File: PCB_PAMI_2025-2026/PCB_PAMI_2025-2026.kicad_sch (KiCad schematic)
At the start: 63 parts, among them J1 BAU, J10 MOTOR 4, J11 COMM_inter_mcu, J12 USB_C_Receptacle_USB2.0_16P, J13 BOOST_OUT, J2 BAT+, J3 VIN_Connector, J4 BAT-, J6 BOOST_IN, J7 MOTOR 3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

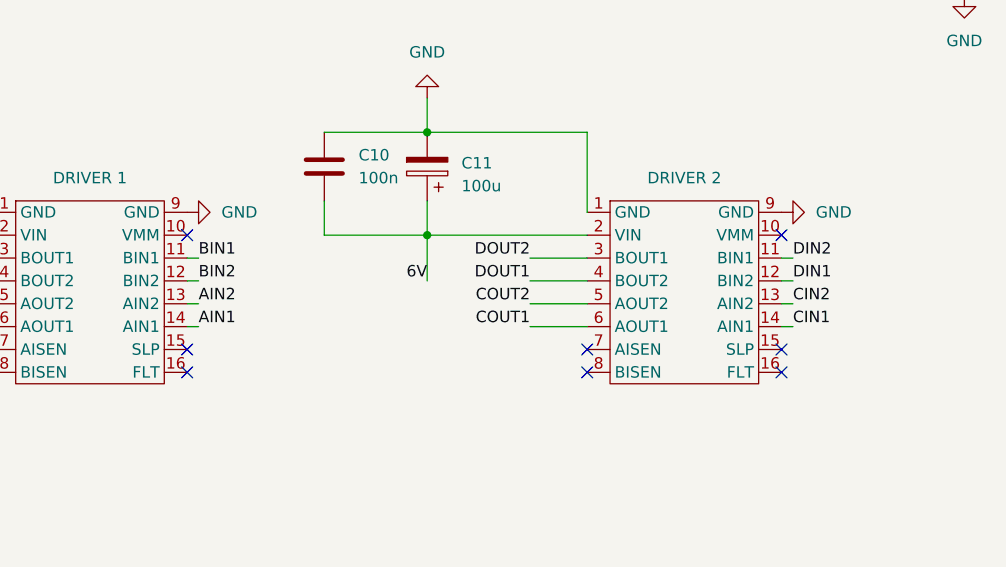
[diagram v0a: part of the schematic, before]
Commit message: correction schéma driver + rajout via gnd
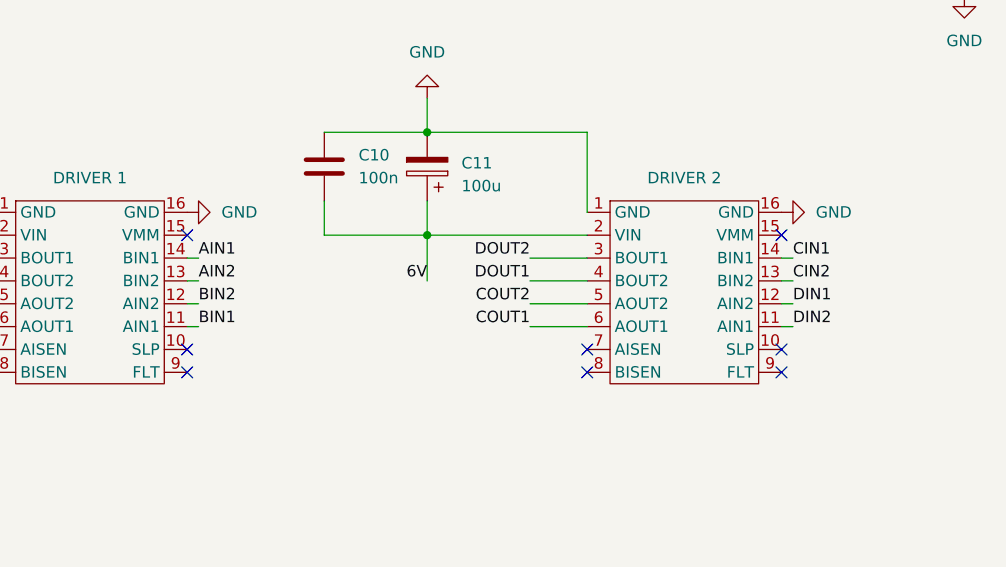
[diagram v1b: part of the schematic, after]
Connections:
- net GND: now also U2.16 (GND), U6.16 (GND); no longer U2.9 (GND), U6.9 (GND)
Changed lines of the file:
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@@
 		)
 	)
-	(label "BIN2"
+	(label "AIN2"
 		(at 140.97 146.05 0)
 		(effects
@@
 		)
 	)
-	(label "AIN1"
+	(label "BIN1"
 		(at 140.97 151.13 0)
 		(effects
@@
 		)
 	)
-	(label "BIN1"
+	(label "AIN1"
 		(at 140.97 143.51 0)
 		(effects
@@
 		)
 	)
-	(label "CIN2"
+	(label "DIN1"
 		(at 207.01 148.59 0)
 		(effects
@@
 		)
 	)
-	(label "AIN2"
+	(label "BIN2"
 		(at 140.97 148.59 0)
 		(effects
@@
 		)
 	)
-	(label "CIN1"
+	(label "DIN2"
 		(at 207.01 151.13 0)
 		(effects
@@
 		)
 	)
-	(label "DIN1"
+	(label "CIN2"
 		(at 207.01 146.05 0)
 		(effects
@@
 		)
 	)
-	(label "DIN2"
+	(label "CIN1"
 		(at 207.01 143.51 0)
 		(effects
@@
 	)
 	(symbol
+		(lib_name "DRV8833_1")
 		(lib_id "ESP_32_ANGE:DRV8833")
 		(at 194.31 143.51 0)
